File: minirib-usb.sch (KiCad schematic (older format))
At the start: 48 parts, among them J1 USB_B_Micro, J2 Mini-DIN-6-Shielded, Q1 MMST3904-7-F, Q2 MMST3906-7-F, Q3 MMST3906-7-F, Q4 MMST3904-7-F, Q5 MMST3904-7-F, Q6 MMST3904-7-F, Q7 MMST3904-7-F, U1 FT231XS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

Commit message: finalized schematic for real this time
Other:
- moved on the sheet: U1
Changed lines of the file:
@@
 L Interface_USB:FT231XS U1
 U 1 1 60FEEDA0
-P 12250 2500
-F 0 "U1" H 12250 2550 50  0000 C CNN
-F 1 "FT231XS" H 12250 2450 50  0000 C CNN
-F 2 "Package_SO:SSOP-20_3.9x8.7mm_P0.635mm" H 13250 1700 50  0001 C CNN
-F 3 "https://www.ftdichip.com/Support/Documents/DataSheets/ICs/DS_FT231X.pdf" H 12250 2500 50  0001 C CNN
-	1    12250 2500
+P 3600 3000
+F 0 "U1" H 3600 3050 50  0000 C CNN
+F 1 "FT231XS" H 3600 2950 50  0000 C CNN
+F 2 "Package_SO:SSOP-20_3.9x8.7mm_P0.635mm" H 4600 2200 50  0001 C CNN
+F 3 "https://www.ftdichip.com/Support/Documents/DataSheets/ICs/DS_FT231X.pdf" H 3600 3000 50  0001 C CNN
+	1    3600 3000
 	1    0    0    -1
 $EndComp

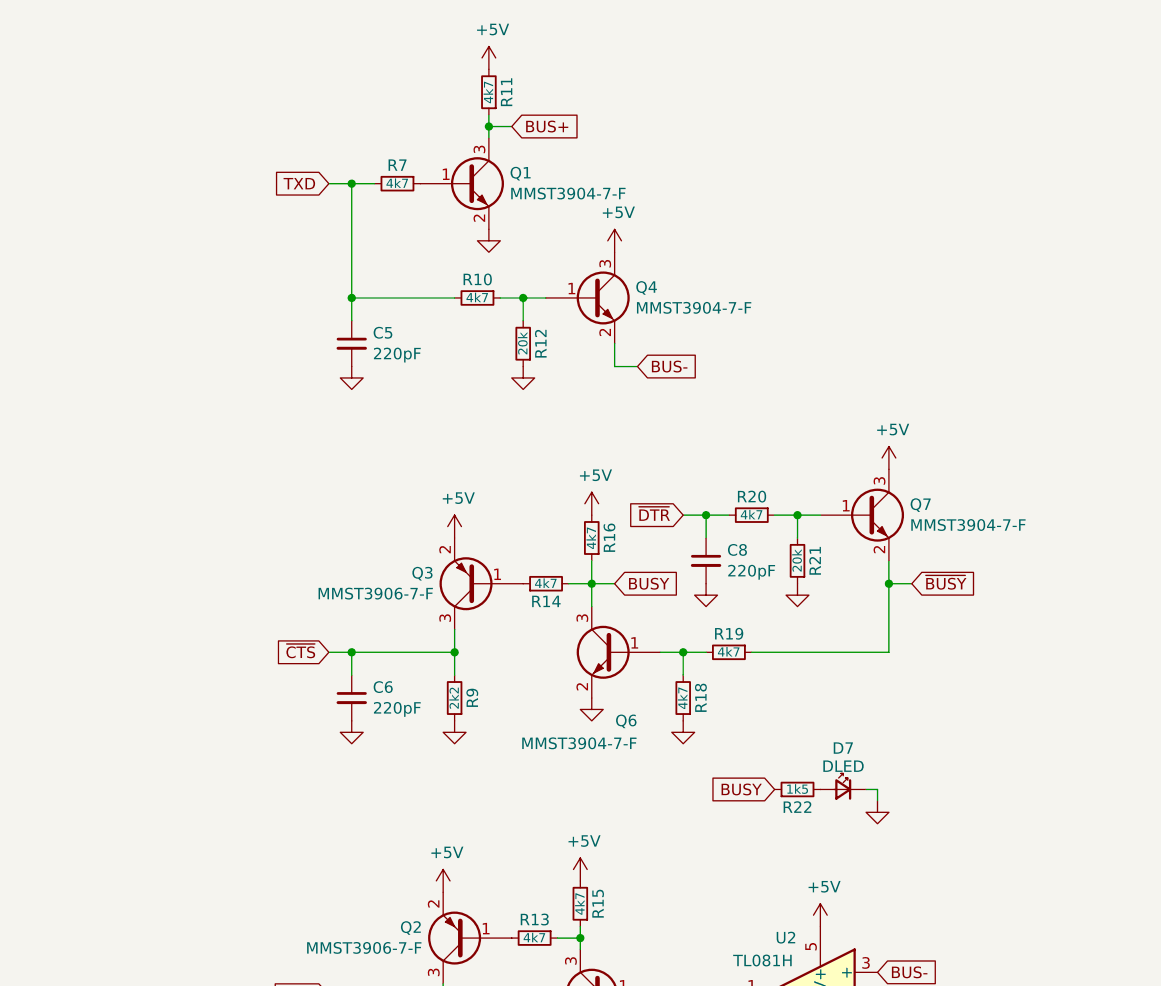
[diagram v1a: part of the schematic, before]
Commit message: converted to Kicad 6 project
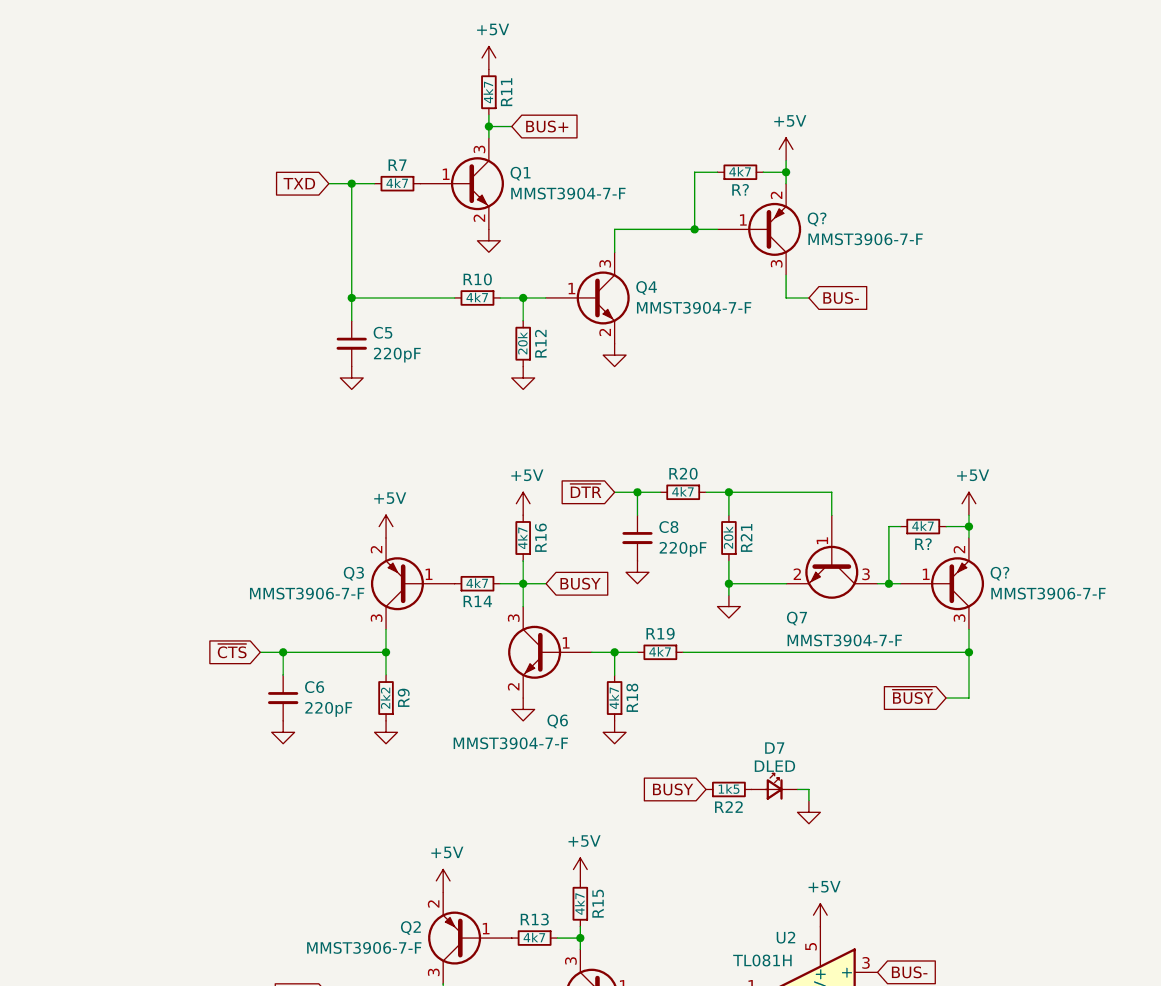
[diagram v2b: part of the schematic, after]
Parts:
- added Q? (x2): MMST3906-7-F, Package_TO_SOT_SMD:SOT-323_SC-70_Handsoldering, symbol Device:Q_PNP_BEC
- added R? (x2): 4k7, Resistor_SMD:R_0805_2012Metric_Pad1.20x1.40mm_HandSolder, symbol Device:R_Small
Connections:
- net +5V: now also Q?.2 (E), Q?.2 (E), R?.2, R?.2; no longer Q4.3 (C), Q7.3 (C)
- net BUS-: now also Q?.3 (C); no longer Q4.2 (E)
- net GND: now also Q4.2 (E), Q7.2 (E)
- net ~BUSY: now also Q?.3 (C); no longer Q7.2 (E)
- new net: Q4.3 (C), Q?.1 (B), R?.1
- new net: Q7.3 (C), Q?.1 (B), R?.1
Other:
- moved on the sheet: C6, C8, D7, Q3, Q6, Q7, R14, R16, R18, R19, R20, R21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
